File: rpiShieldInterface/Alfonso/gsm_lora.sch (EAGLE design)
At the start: 54 parts, among them Q1 MUN2213T1, Q2 MUN2213T1, Q3 MUN2213T1

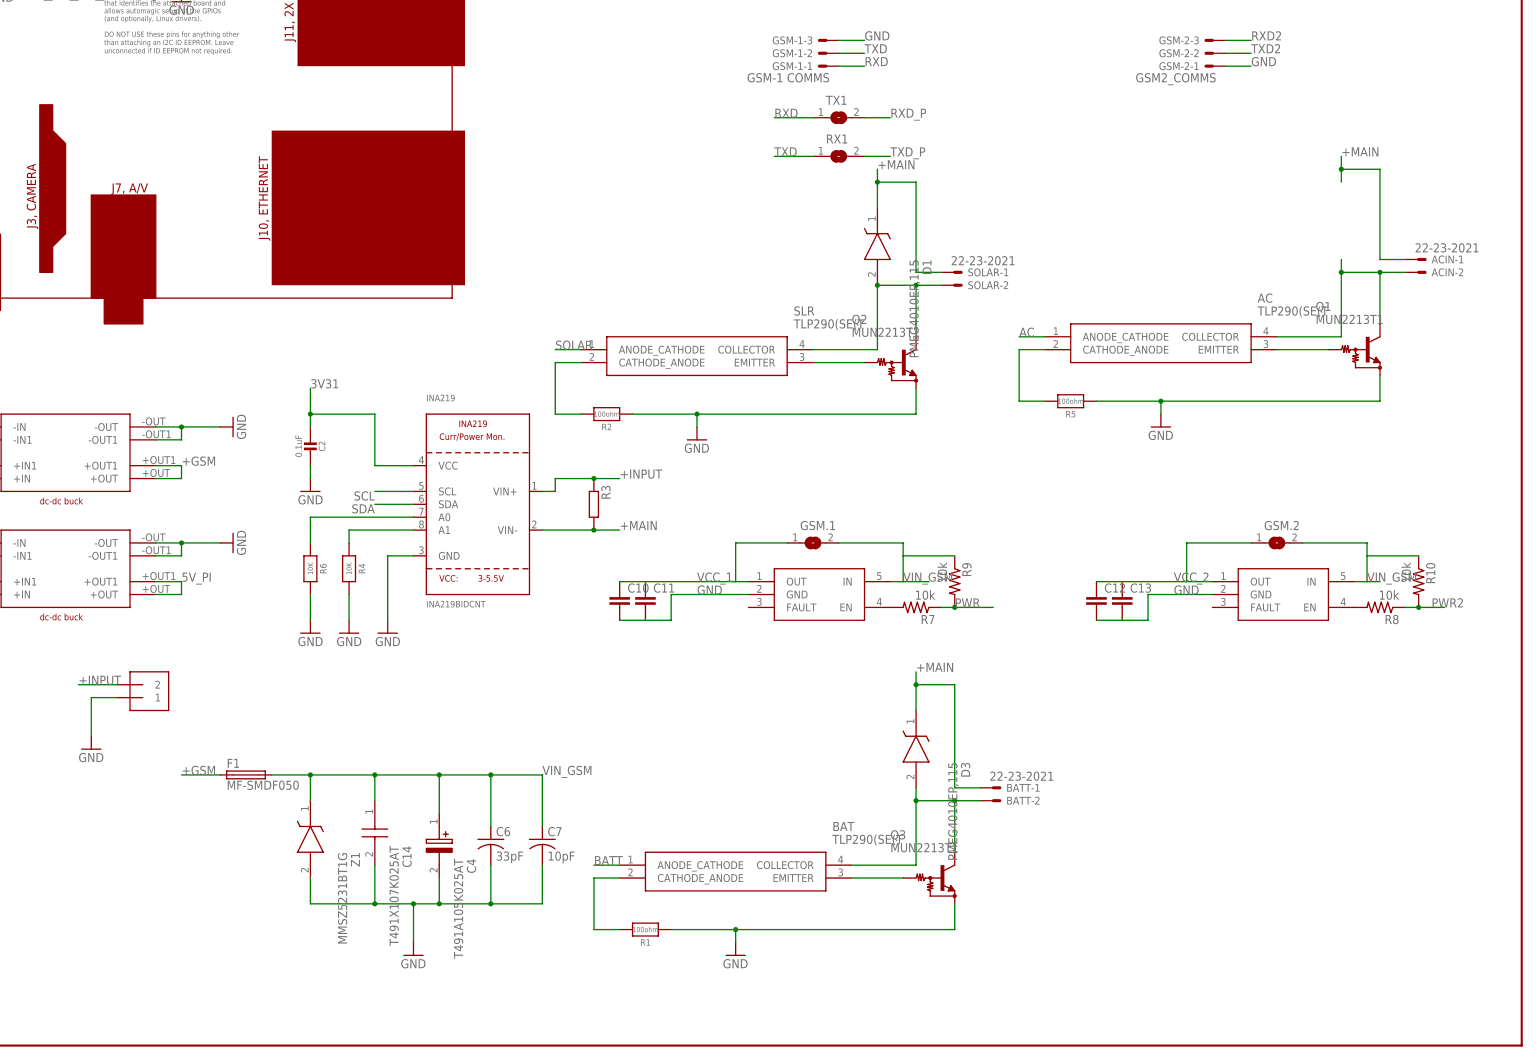
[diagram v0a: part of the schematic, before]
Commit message: updated schematic and layout for switching function added CAMOutputs
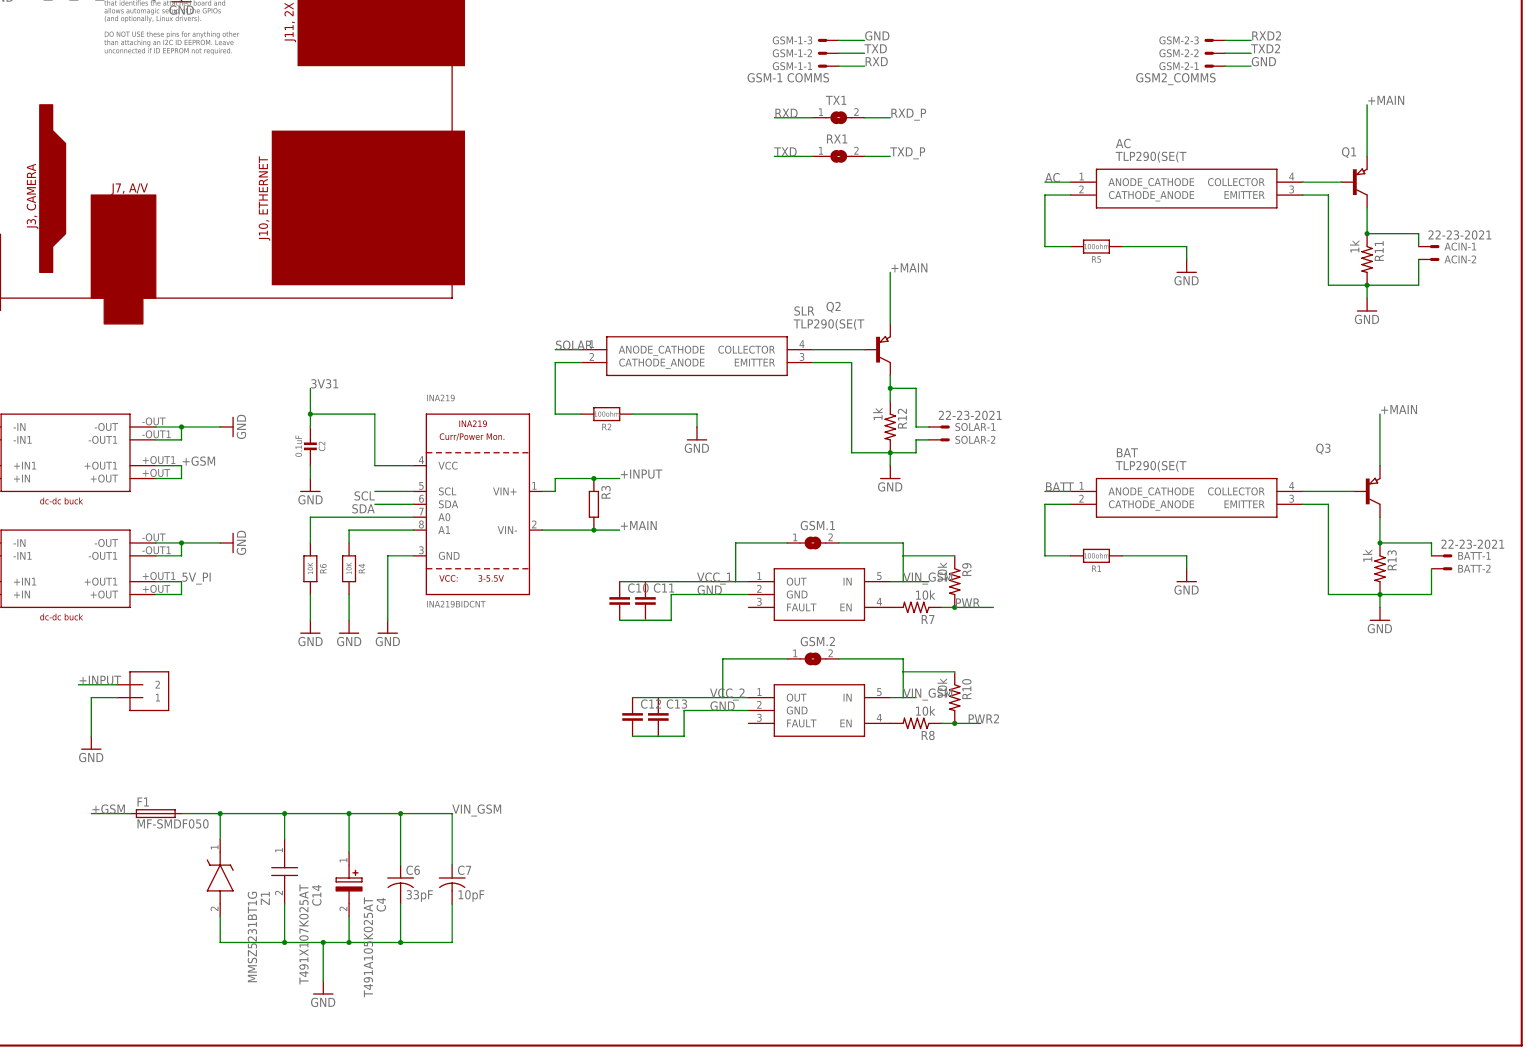
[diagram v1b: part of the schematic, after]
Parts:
- removed D1, D3: PMEG4010EP,115, PMEG4010EP_115:PMEG4010EP,115
- added R11, R12, R13: 1k, rcl:R-US_R0805
- Q1, Q2, Q3: value MUN2213T1 -> (none); device transistor-npn:MUN2213T1 -> semicon-smd-ipc:PNP-TRANSISTOR_SOT23
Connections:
- net +MAIN: now also Q1.E, Q2.E, Q3.E; no longer ACIN-1.S, BATT-1.S, D1.K, D3.K, SOLAR-1.S
- net GND: now also AC.EMITTER, ACIN-2.S, BAT.EMITTER, BATT-2.S, R11.2, R12.2, R13.2, SLR.EMITTER, SOLAR-2.S; no longer Q1.E, Q2.E, Q3.E
- net N$10: now also Q3.B; no longer BATT-2.S, D3.A, Q3.C
- net N$11: now also SLR.COLLECTOR; no longer SLR.EMITTER
- net N$12: now also BATT-1.S, Q3.C, R13.1; no longer BAT.EMITTER, Q3.B
- net N$18: now also Q2.C, R12.1, SOLAR-1.S; no longer AC.COLLECTOR, ACIN-2.S, Q1.C
- net N$7: now also AC.COLLECTOR; no longer AC.EMITTER
- net N$8: now also ACIN-1.S, Q1.C, R11.1; no longer D1.A, Q2.C, SLR.COLLECTOR, SOLAR-2.S
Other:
- moved on the sheet: AC, ACIN-1, ACIN-2, BAT, BATT-1, BATT-2, C12, C13, C14, C4, C6, C7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

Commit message: added ptc fuse from 5V out to rpi
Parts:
- added F2: MF-SMDF050, fuse:MF-SMDF050
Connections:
- new net N$23: F2.1, U$4.+OUT, U$4.+OUT1
- net 5V_PI: now also F2.2; no longer U$4.+OUT, U$4.+OUT1
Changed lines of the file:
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@@
 <part name="R13" library="rcl" library_urn="urn:adsk.eagle:library:334" deviceset="R-US_" device="R0805" package3d_urn="urn:adsk.eagle:package:23553/2" value="1k"/>
 <part name="GND29" library="supply1" library_urn="urn:adsk.eagle:library:371" deviceset="GND" device=""/>
+<part name="F2" library="fuse" library_urn="urn:adsk.eagle:library:233" deviceset="MF-SMDF" device="" package3d_urn="urn:adsk.eagle:package:14081/1" technology="050"/>
 </parts>
 <sheets>
@@
 <instance part="GND29" gate="1" x="373.38" y="83.82">
 <attribute name="VALUE" x="370.84" y="81.28" size="1.778" layer="96"/>
+</instance>
+<instance part="F2" gate="A" x="142.24" y="91.44">
+<attribute name="NAME" x="138.43" y="92.837" size="1.778" layer="95"/>
+<attribute name="VALUE" x="138.43" y="88.519" size="1.778" layer="96"/>
 </instance>
 </instances>
@@
 </segment>
 <segment>
-<pinref part="U$4" gate="G$1" pin="+OUT1"/>
-<wire x1="132.08" y1="91.44" x2="137.16" y2="91.44" width="0.1524" layer="91"/>
-<wire x1="137.16" y1="91.44" x2="137.16" y2="88.9" width="0.1524" layer="91"/>
-<pinref part="U$4" gate="G$1" pin="+OUT"/>
-<wire x1="137.16" y1="88.9" x2="132.08" y2="88.9" width="0.1524" layer="91"/>
-<label x="137.16" y="91.44" size="1.778" layer="95"/>
+<pinref part="F2" gate="A" pin="2"/>
+<wire x1="147.32" y1="91.44" x2="152.4" y2="91.44" width="0.1524" layer="91"/>
+<label x="152.4" y="91.44" size="1.778" layer="95"/>
 </segment>
 </net>
@@
 </segment>
 </net>
+<net name="N$23" class="0">
+<segment>
+<pinref part="U$4" gate="G$1" pin="+OUT1"/>
+<pinref part="F2" gate="A" pin="1"/>
+<wire x1="132.08" y1="91.44" x2="137.16" y2="91.44" width="0.1524" layer="91"/>
+<pinref part="U$4" gate="G$1" pin="+OUT"/>
+<wire x1="132.08" y1="88.9" x2="137.16" y2="88.9" width="0.1524" layer="91"/>
+<wire x1="137.16" y1="88.9" x2="137.16" y2="91.44" width="0.1524" layer="91"/>
+<junction x="137.16" y="91.44"/>
+</segment>
+</net>
